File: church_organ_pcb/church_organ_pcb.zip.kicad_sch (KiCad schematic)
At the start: 50 parts, among them J1 4.5-28V Power Input, J2 USB, J3 Fan 1, J4 Fan 2, J5 Conn_01x13_Socket, J6 Conn_01x13_Socket, U1 AP63205WU, U4 SN74HC125DR, U5 CH340C, U6 AMS1117-3.3, U7 AMS1117-3.3, U8 SN74HC125DR

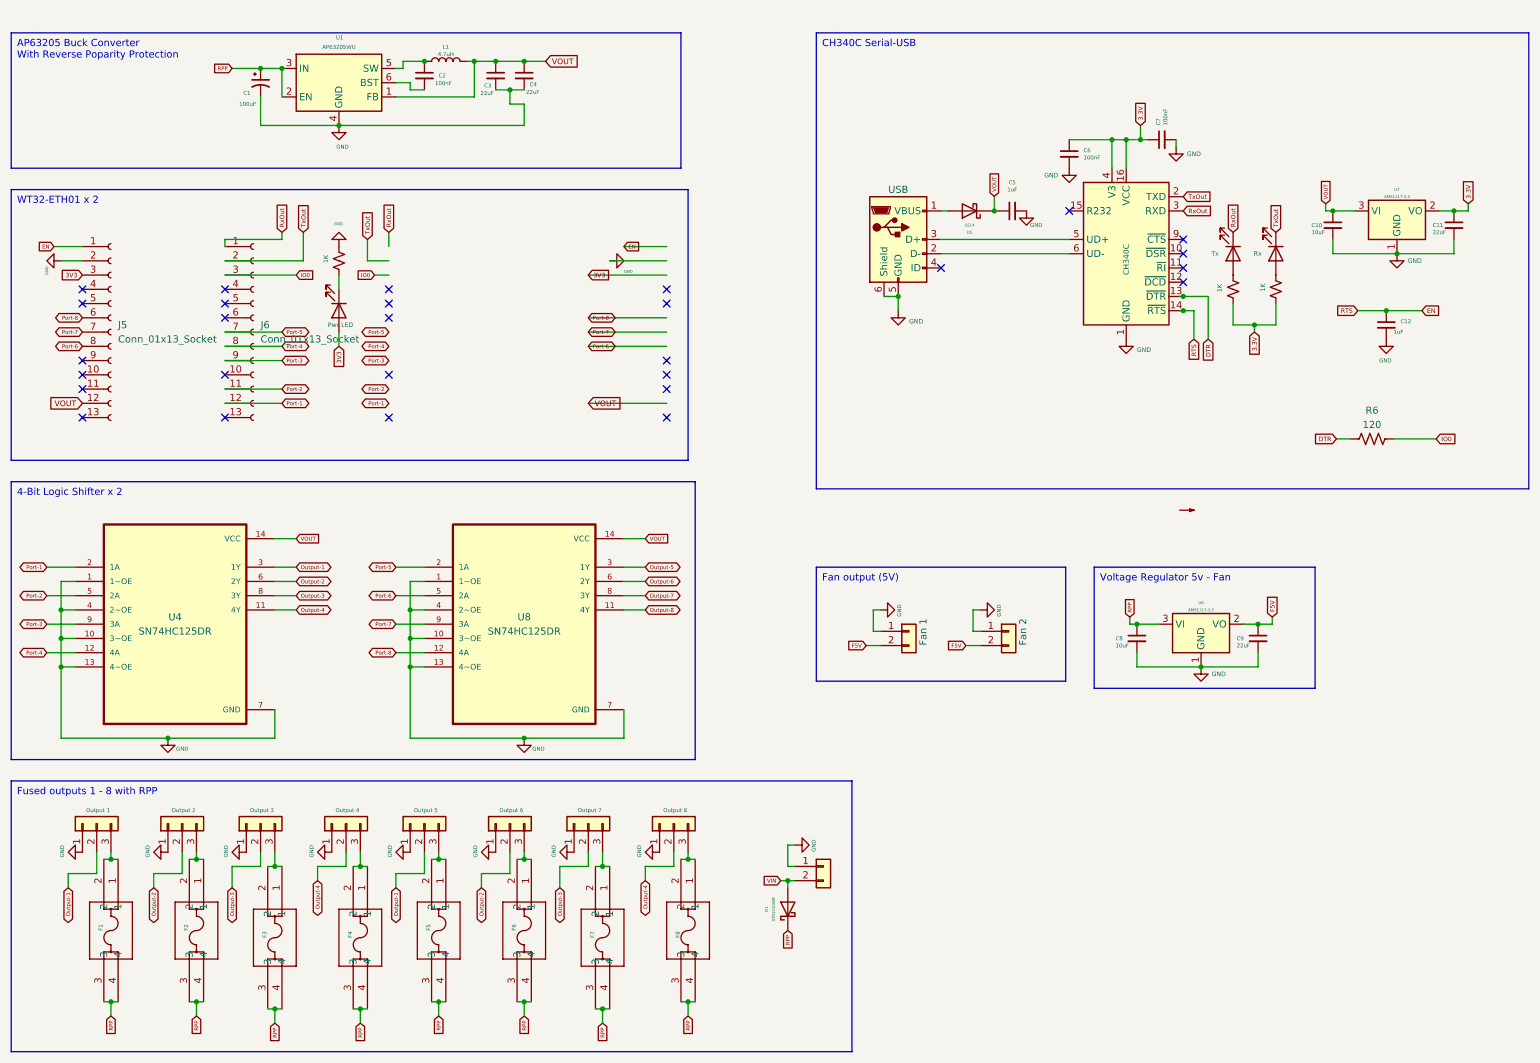
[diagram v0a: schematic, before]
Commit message: removed fan outputs and regulator, fixed traces and removed esp32s, made holes bigger for screws
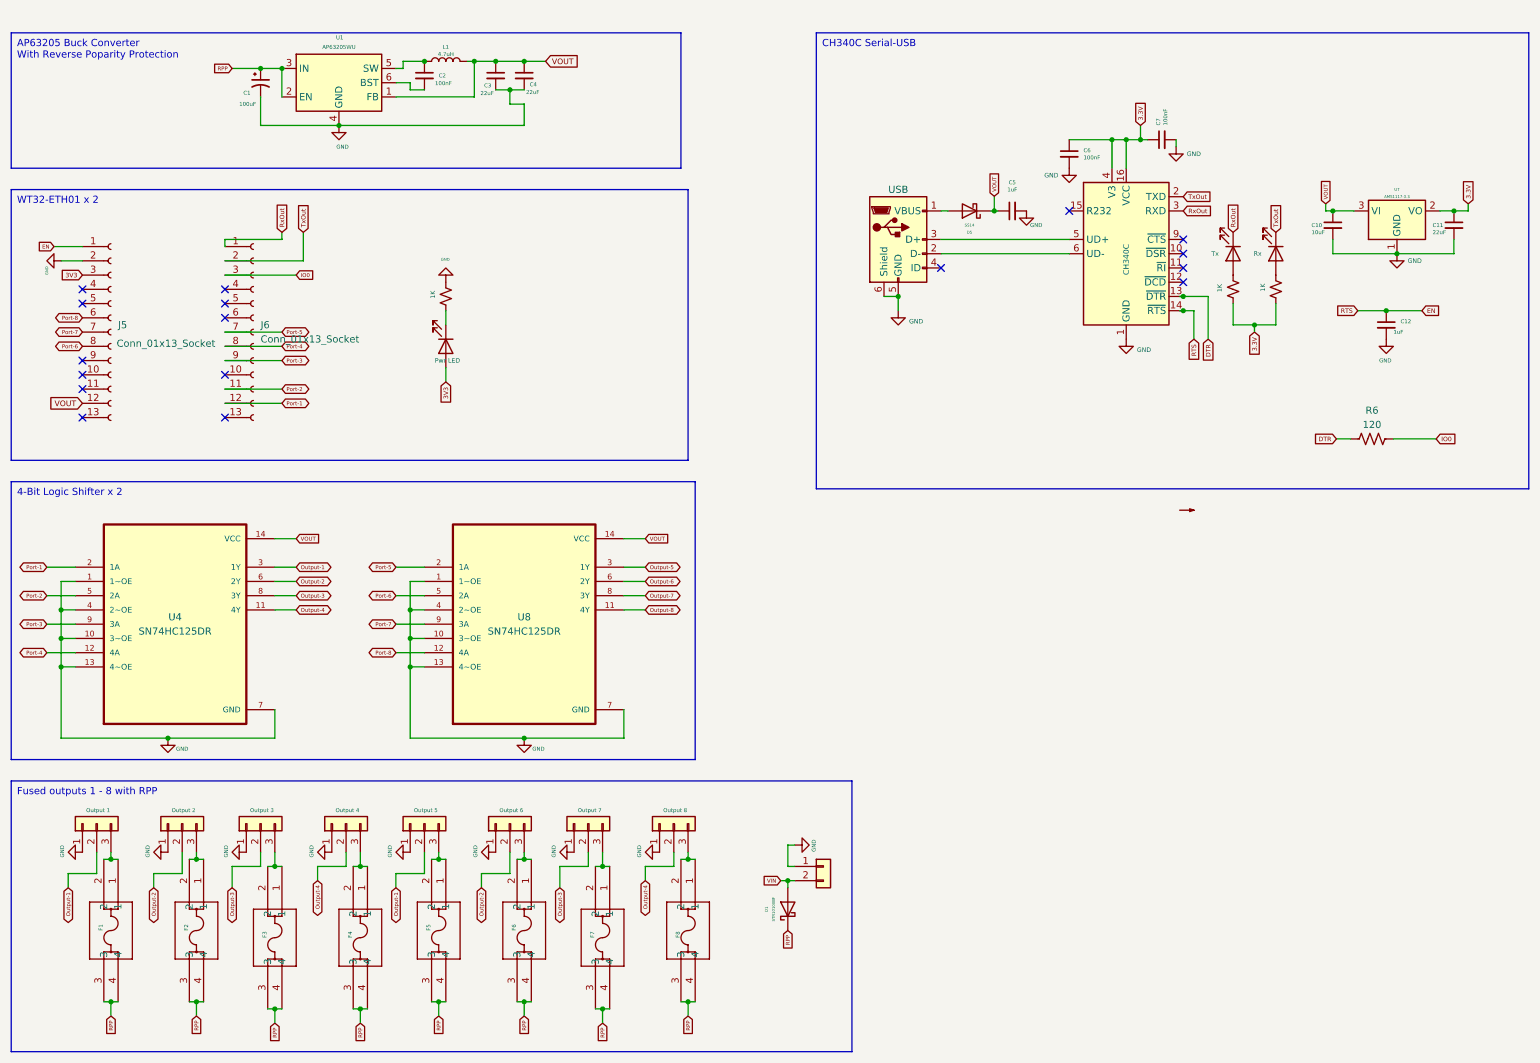
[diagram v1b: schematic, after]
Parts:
- removed C8: 10uF, Capacitor_SMD:C_0805_2012Metric_Pad1.18x1.45mm_HandSolder, symbol Device:C_Small
- removed C9: 22uF, Capacitor_SMD:C_0805_2012Metric_Pad1.18x1.45mm_HandSolder, symbol Device:C_Small
- removed J3: Fan 1, Connector_JST:JST_XH_B2B-XH-A_1x02_P2.50mm_Vertical, symbol Connector_Generic:Conn_01x02
- removed J4: Fan 2, Connector_JST:JST_XH_B2B-XH-A_1x02_P2.50mm_Vertical, symbol Connector_Generic:Conn_01x02
- removed U6: AMS1117-3.3, Package_TO_SOT_SMD:SOT-223-3_TabPin2, symbol Regulator_Linear:AMS1117-3.3
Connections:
- no-connect marks 28 -> 17

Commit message: schema edited
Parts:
- JST1: Mfg Part# (none) -> 1711738
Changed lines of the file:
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@@
+			)
+		)
+		(property "Mfg Part#" "1711738"
+			(at 29.21 156.21 0)
+			(effects
+				(font
+					(size 1.27 1.27)
+				)
+				(hide yes)
 			)
 		)

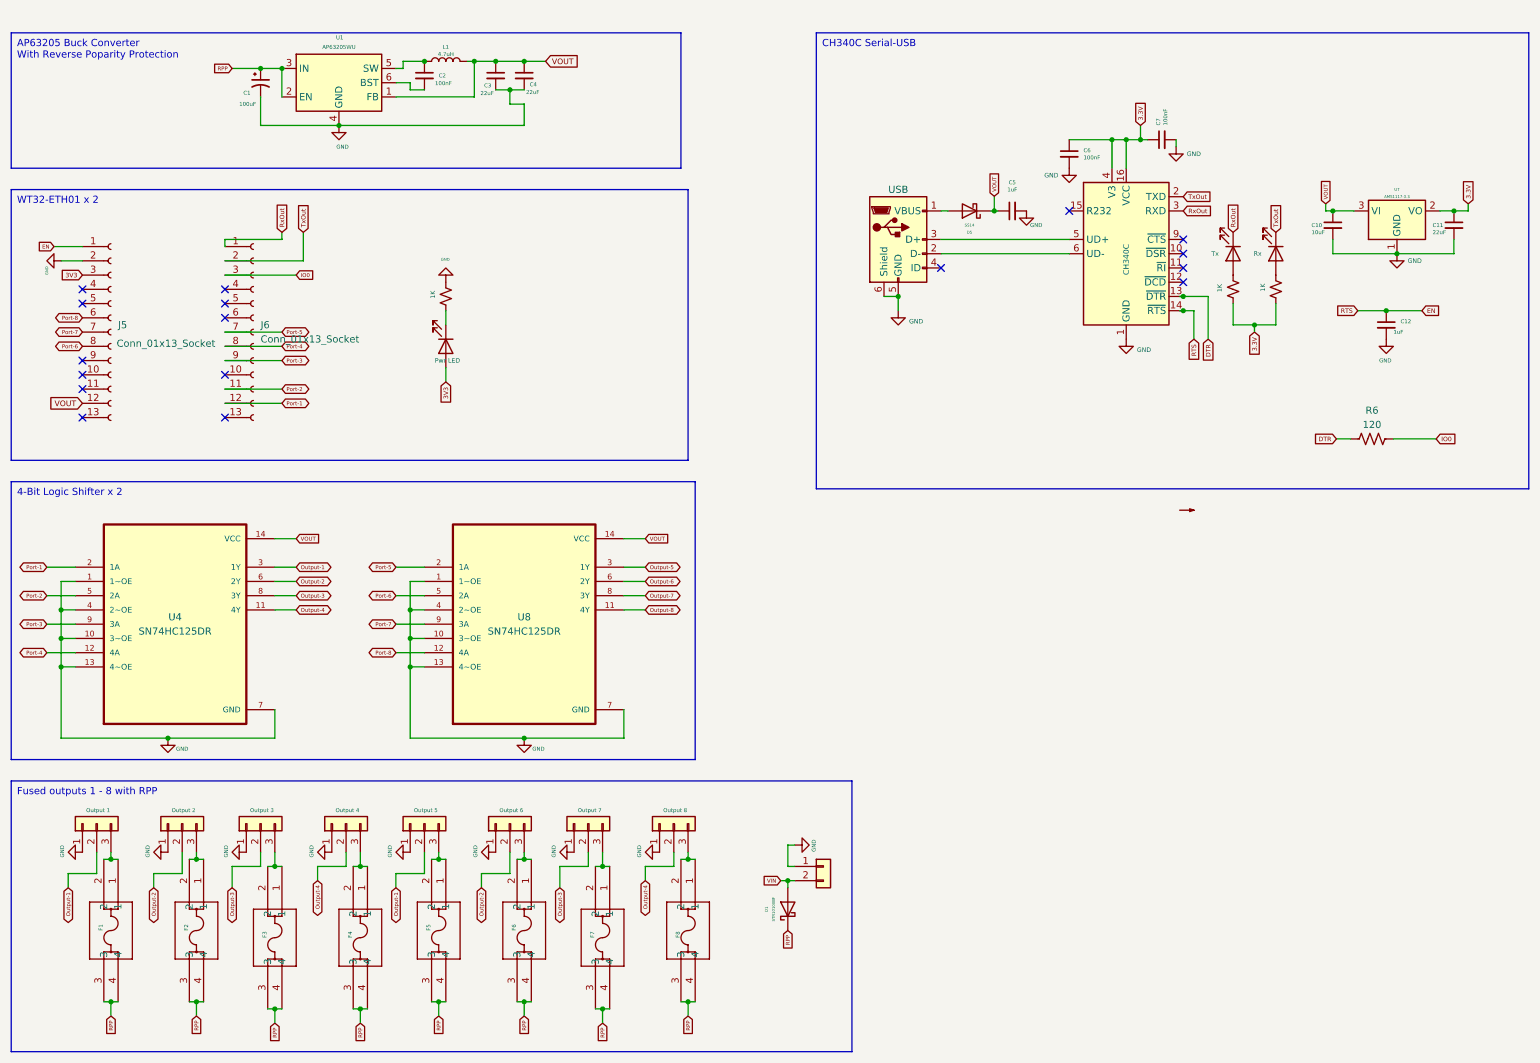
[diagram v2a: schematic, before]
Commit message: Commit changes to PCB
Rerouted power traces to/from the fuses
Replaced screw terminal with quick connect terminals
Fixed an issue where LED-outputs 5,6,7,8 was not correctly connected to their NETs
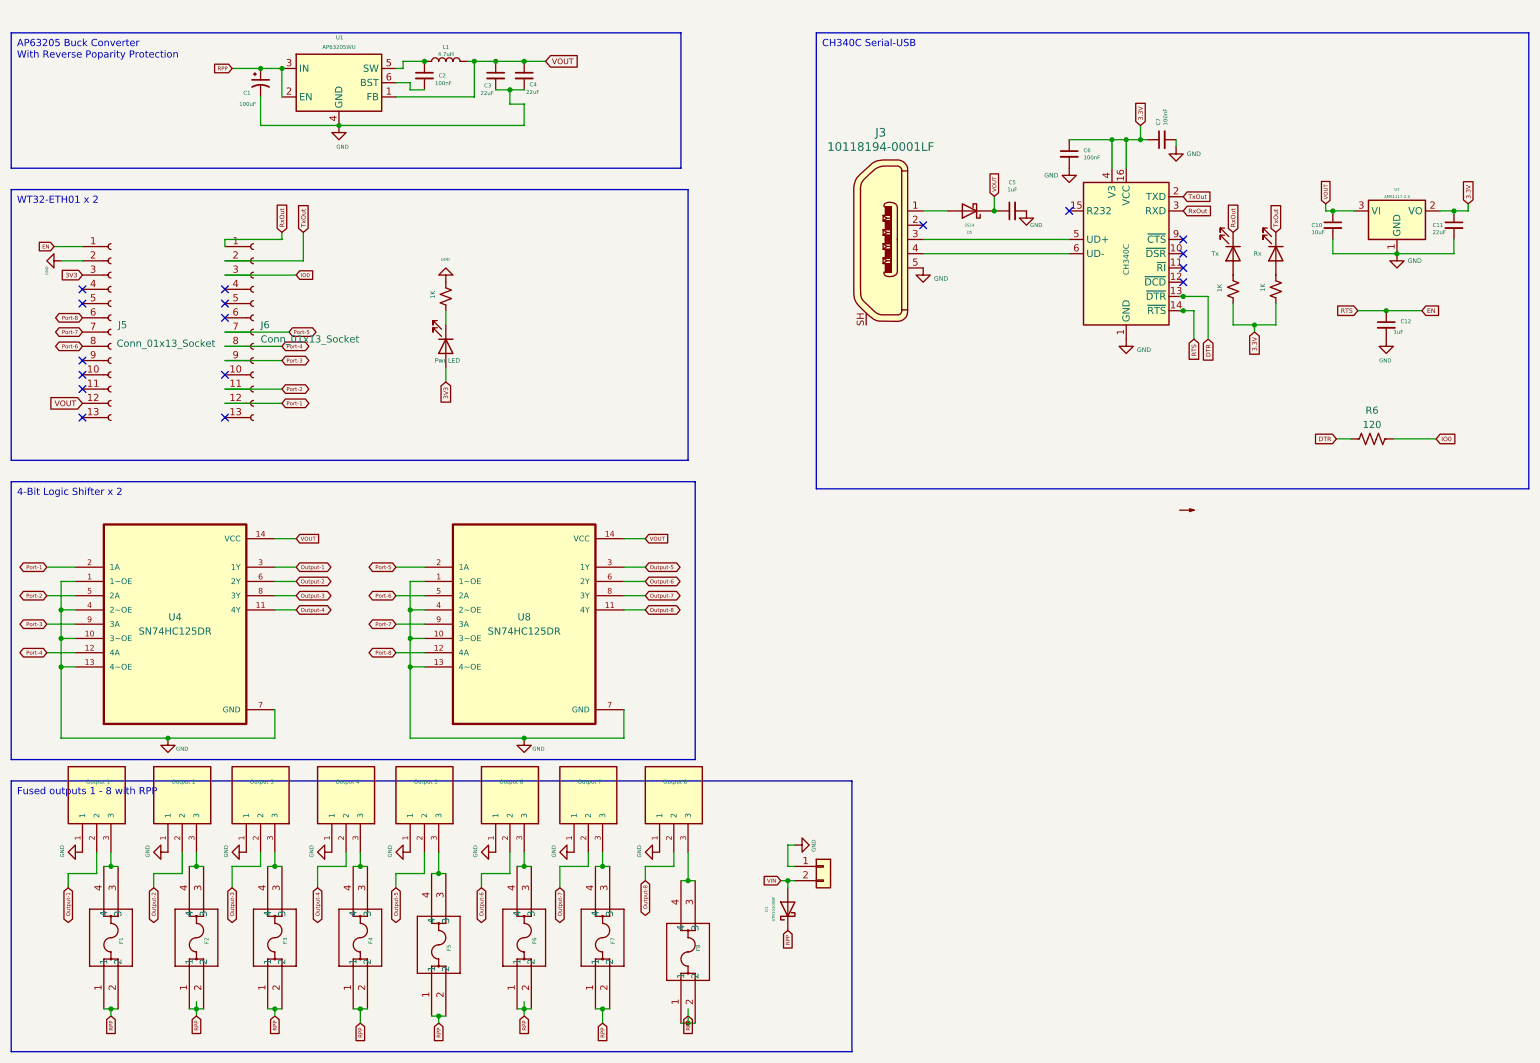
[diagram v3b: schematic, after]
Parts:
- removed J2: USB, MicroUSB:USB_Micro-B_Unknown_5s_SMT, symbol Connector:USB_B_Micro
- added J3: 10118194-0001LF, digikey-footprints:USB_Micro_B_Female_10118194-0001LF, symbol dk_USB-DVI-HDMI-Connectors:10118194-0001LF
- F1, F2, F3, F4, F5, F6, F7, F8: footprint WT32-ETH-Fuse-Holder:MCCQ-122_MTC -> 3544-fuse:CONN_3544-2_KEY
- J1: footprint SamacSys_Parts:1714955 -> terminal_block_footprints:CONN_691321300002_WRE
- JST1, JST2, JST3, JST4, JST5, JST6, JST7, JST8: footprint TerminalBlock_Phoenix:TerminalBlock_Phoenix_MKDS-1,5-3-5.08_1x03_P5.08mm_Horizontal -> 3pin:CUI_TBP02R2-381-03BE; symbol Connector_Generic:Conn_01x03 -> TBP02R2-381-03BE:TBP02R2-381-03BE; MANUFACTURER (none) -> CUI; STANDARD (none) -> Manufacturer Recommendations
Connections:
- net GND: now also J3.5
- net Output-1: no longer JST5.2 (Pin_2)
- net Output-2: no longer JST6.2 (Pin_2)
- net Output-3: no longer JST7.2 (Pin_2)
- net Output-4: no longer JST8.2 (Pin_2)
- net Output-5: now also JST5.2
- net Output-6: now also JST6.2
- net Output-7: now also JST7.2
- net Output-8: now also JST8.2
- net RPP: now also F1.1, F1.2, F2.1, F2.2, F3.1, F3.2, F4.1, F4.2, F5.1, F5.2, F6.1, F6.2, F7.1, F7.2, F8.1, F8.2; no longer F1.3, F1.4, F2.3, F2.4, F3.3, F3.4, F4.3, F4.4, F5.3, F5.4, F6.3, F6.4, F7.3, F7.4, F8.3, F8.4
- net at D5.2 (A): now also J3.1
- net at U5.6 (UD-): now also J3.4
- net at U5.5 (UD+): now also J3.3
- new net: F7.3, F7.4, JST7.3
- new net: F8.3, F8.4, JST8.3
- new net: F4.3, F4.4, JST4.3
- new net: F1.3, F1.4, JST1.3
- new net: F3.3, F3.4, JST3.3
- new net: F6.3, F6.4, JST6.3
- new net: F2.3, F2.4, JST2.3
- new net: F5.3, F5.4, JST5.3
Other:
- moved on the sheet: F1, F2, F3, F4, F5, F6, F7, F8

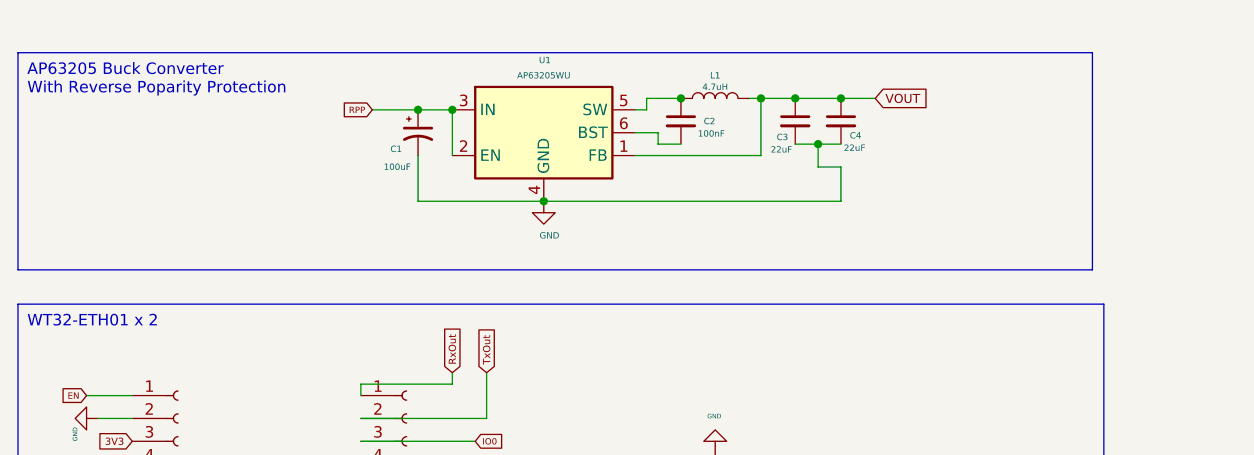
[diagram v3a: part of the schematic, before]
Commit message: Add new 4.7mH inductor to voltage regulator circuit + fix 3d models
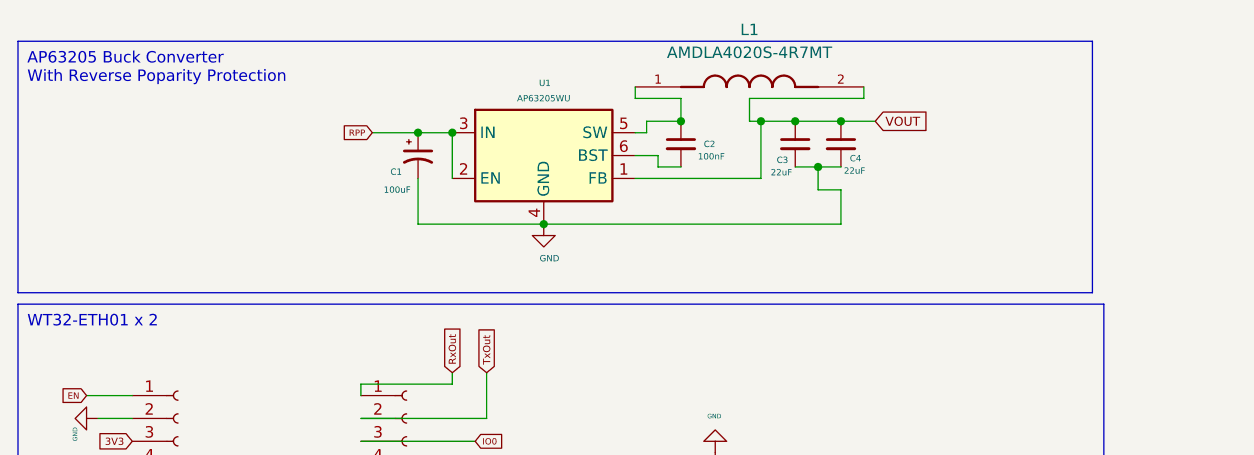
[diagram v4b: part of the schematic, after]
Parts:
- removed L1: 4.7uH, Inductor_SMD:L_Taiyo-Yuden_MD-5050, symbol Device:L
- added L1: AMDLA4020S-4R7MT, AMDLA4020S-4R7MT:IND_AMDLA4020S-4R7MT, symbol AMDLA4020S:AMDLA4020S-4R7MT
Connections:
- net VOUT: now also L1.2
- net at C2.1, U1.5 (SW): now also L1.1
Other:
- moved on the sheet: C1, C2, C3, C4, U1
